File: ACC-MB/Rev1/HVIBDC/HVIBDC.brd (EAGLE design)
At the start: 100.2 x 48.2 mm, 34 parts, among them IC1 555

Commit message: update
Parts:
- added LED2, LED3, LED4, LED5: (no value), ACC-MB-R0:LED3MM
- added R13, R14, R15, R18: (no value), ACC-MB-R0:R0805
- moved U$2 9.06 mm to (-3.00, 17.0)
- moved U$14 6.79 mm to (0.70, 27.5), turned to 90 degrees
- moved U$1 1.00 mm to (66.0, 17.0)
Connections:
- new net N$17: LED2.K, R13.2
- new net N$19: LED3.K, R14.2
- new net N$25: LED4.K, R15.2
- new net N$27: LED5.K, R18.2
- net +12V: now also LED2.A, LED3.A, LED4.A, LED5.A
- net ACC_LGHT: now also R13.1
- net GND: now also R18.1
- net TSAL_GRN_GND: now also R14.1
- net TSAL_RED_GND: now also R15.1
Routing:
- net ACC_LGHT: track 50.5 -> 84.4 mm
- net TSAL_GRN_GND: track 73.5 -> 89.8 mm
- net TSAL_RED_GND: track 55.0 -> 68.1 mm
- net N$7: track 22.9 -> 34.6 mm
- net N$17: track 0.00 -> 8.95 mm
- net N$27: track 0.00 -> 5.57 mm
- net N$22: track 4.07 -> 8.62 mm
- net N$13: track 45.9 -> 50.0 mm
- net N$25: track 0.00 -> 3.74 mm
- net N$19: track 0.00 -> 3.32 mm
- net V-: track 58.9 -> 59.9 mm
- net V+: track 27.8 -> 28.8 mm
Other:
- board size 100.2 x 48.2 mm -> 92.2 x 49.2 mm

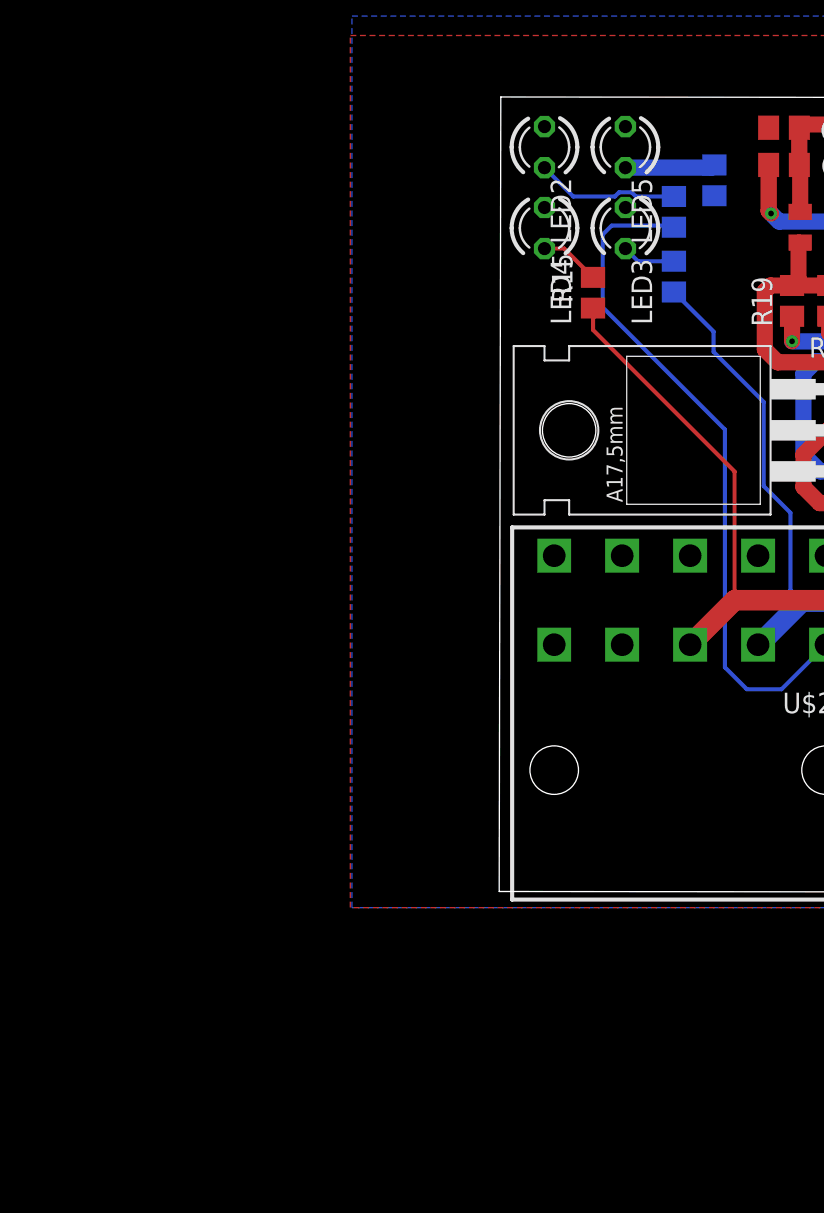
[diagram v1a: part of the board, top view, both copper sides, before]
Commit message: 7792 added to all DC
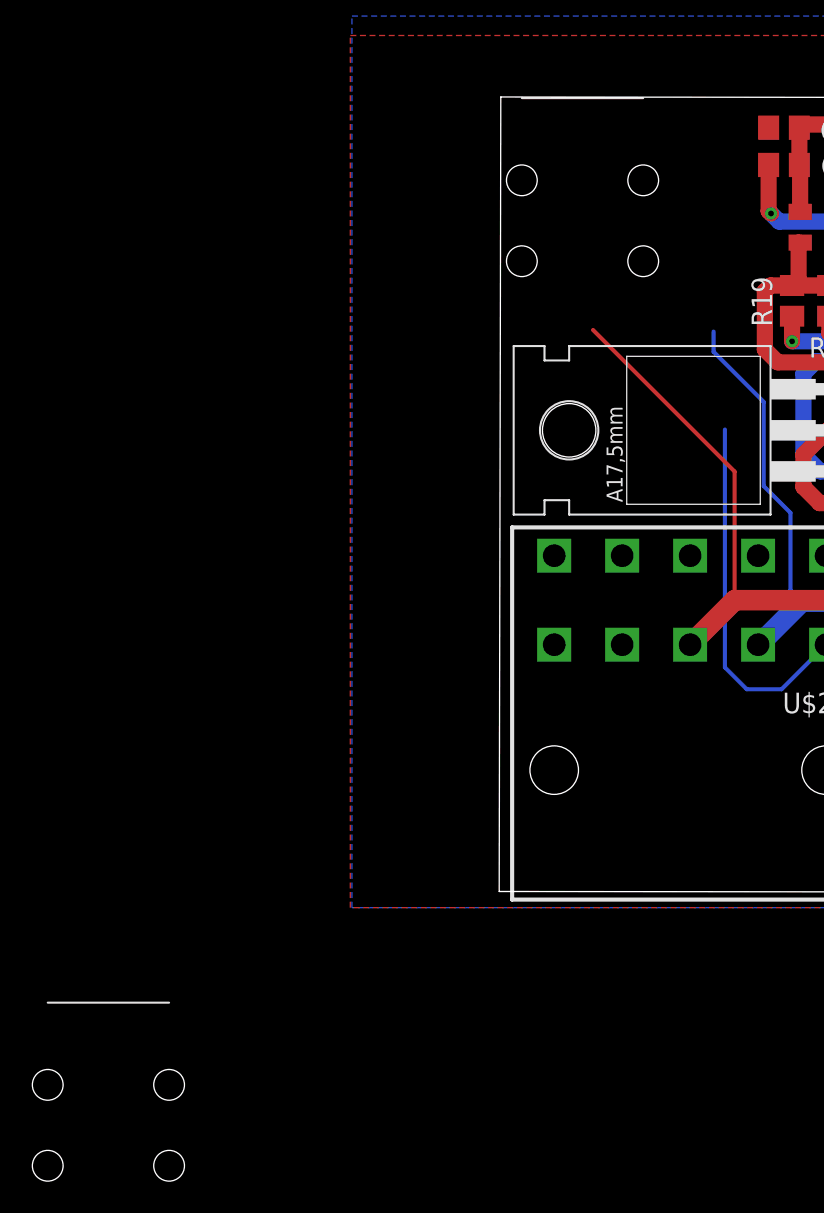
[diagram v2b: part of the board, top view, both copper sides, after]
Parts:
- removed LED2, LED3, LED4, LED5: (no value), ACC-MB-R0:LED3MM
- removed R13, R14, R15, R18: (no value), ACC-MB-R0:R0805
- added U$3, U$4: 7792, ACC-MB-R0:7792
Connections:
- removed net N$17: LED2.K, R13.2
- removed net N$19: LED3.K, R14.2
- removed net N$25: LED4.K, R15.2
- removed net N$27: LED5.K, R18.2
- net +12V: no longer LED2.A, LED3.A, LED4.A, LED5.A
- net ACC_LGHT: no longer R13.1
- net GND: no longer R18.1
- net TSAL_GRN_GND: no longer R14.1
- net TSAL_RED_GND: no longer R15.1
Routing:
- net ACC_LGHT: track 84.4 -> 64.5 mm
- net N$17: track 8.95 -> 0.00 mm
- net N$27: track 5.57 -> 0.00 mm
- net N$25: track 3.74 -> 0.00 mm
- net TSAL_GRN_GND: track 89.8 -> 86.3 mm
- net N$19: track 3.32 -> 0.00 mm
- net TSAL_RED_GND: track 68.1 -> 66.8 mm
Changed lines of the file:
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@@
 <drawing>
 <settings>
-<setting alwaysvectorfont="yes"/>
+<setting alwaysvectorfont="no"/>
 <setting verticaltext="up"/>
 </settings>
@@
 <element name="U$2" library="ACC-MB-R0" library_urn="urn:adsk.eagle:library:13208985" package="15-24-6100" package3d_urn="urn:adsk.eagle:package:14396594/2" value="15-24-6100" x="-3" y="17"/>
 <element name="U$1" library="ACC-MB-R0" library_urn="urn:adsk.eagle:library:13208985" package="15-24-6100" package3d_urn="urn:adsk.eagle:package:14396594/2" value="15-24-6100" x="66" y="17"/>
-<element name="LED2" library="ACC-MB-R0" library_urn="urn:adsk.eagle:library:13208985" package="LED3MM" package3d_urn="urn:adsk.eagle:package:15797/1" value="" x="-12" y="45" rot="R270"/>
-<element name="R13" library="ACC-MB-R0" library_urn="urn:adsk.eagle:library:13208985" package="R0805" package3d_urn="urn:adsk.eagle:package:13209583/1" value="" x="-4" y="41" rot="MR90">
-<attribute name="SPICEPREFIX" value="R" x="-4" y="41" size="1.778" layer="28" rot="MR90" display="off"/>
-</element>
-<element name="LED3" library="ACC-MB-R0" library_urn="urn:adsk.eagle:library:13208985" package="LED3MM" package3d_urn="urn:adsk.eagle:package:15797/1" value="" x="-7" y="40" rot="R270"/>
-<element name="R14" library="ACC-MB-R0" library_urn="urn:adsk.eagle:library:13208985" package="R0805" package3d_urn="urn:adsk.eagle:package:13209583/1" value="" x="-4" y="37" rot="MR90">
-<attribute name="SPICEPREFIX" value="R" x="-4" y="37" size="1.778" layer="28" rot="MR90" display="off"/>
-</element>
-<element name="LED4" library="ACC-MB-R0" library_urn="urn:adsk.eagle:library:13208985" package="LED3MM" package3d_urn="urn:adsk.eagle:package:15797/1" value="" x="-12" y="40" rot="R270"/>
-<element name="R15" library="ACC-MB-R0" library_urn="urn:adsk.eagle:library:13208985" package="R0805" package3d_urn="urn:adsk.eagle:package:13209583/1" value="" x="-9" y="36" rot="R90">
-<attribute name="SPICEPREFIX" value="R" x="-9" y="36" size="1.778" layer="27" rot="R90" display="off"/>
-</element>
-<element name="LED5" library="ACC-MB-R0" library_urn="urn:adsk.eagle:library:13208985" package="LED3MM" package3d_urn="urn:adsk.eagle:package:15797/1" value="" x="-7" y="45" rot="R270"/>
-<element name="R18" library="ACC-MB-R0" library_urn="urn:adsk.eagle:library:13208985" package="R0805" package3d_urn="urn:adsk.eagle:package:13209583/1" value="" x="-1.5" y="42.95" rot="MR90">
-<attribute name="SPICEPREFIX" value="R" x="-1.5" y="42.95" size="1.778" layer="28" rot="MR90" display="off"/>
-</element>
+<element name="U$3" library="ACC-MB-R0" library_urn="urn:adsk.eagle:library:13208985" package="7792" package3d_urn="urn:adsk.eagle:package:14511284/2" value="7792" x="-42.7" y="-17.95"/>
+<element name="U$4" library="ACC-MB-R0" library_urn="urn:adsk.eagle:library:13208985" package="7792" package3d_urn="urn:adsk.eagle:package:14511284/2" value="7792" x="-13.4" y="37.95"/>
 </elements>
 <signals>
@@
 <wire x1="13.9" y1="33" x2="14.19" y2="33.29" width="1" layer="16"/>
 <contactref element="U$2" pad="7"/>
-<contactref element="R18" pad="1"/>
-<wire x1="1.2" y1="19.75" x2="-1.5" y2="42" width="0" layer="19" extent="1-1"/>
-<wire x1="7.05" y1="30.04" x2="1.2" y2="19.75" width="0" layer="19" extent="1-1"/>
-<wire x1="5.5" y1="33" x2="7.05" y2="30.04" width="0" layer="19" extent="16-16"/>
+<wire x1="30.7" y1="45.05" x2="41.4" y2="40" width="0" layer="19" extent="1-16"/>
+<wire x1="28" y1="44.95" x2="30.7" y2="45.05" width="0" layer="19" extent="1-1"/>
+<wire x1="25.05" y1="44.95" x2="28" y2="44.95" width="0" layer="19" extent="1-1"/>
+<wire x1="22" y1="44.95" x2="25.05" y2="44.95" width="0" layer="19" extent="1-1"/>
+<wire x1="19" y1="44.95" x2="22" y2="44.95" width="0" layer="19" extent="1-1"/>
+<wire x1="11.08" y1="36.4" x2="19" y2="44.95" width="0" layer="19" extent="1-16"/>
 <wire x1="7.8" y1="34.55" x2="7.6" y2="35.1" width="0" layer="19" extent="1-16"/>
 <wire x1="1.85" y1="46.2" x2="1.85" y2="43.9" width="0" layer="19" extent="1-1"/>
+<wire x1="7.05" y1="30.04" x2="5.5" y2="33" width="0" layer="19" extent="16-16"/>
 <wire x1="13.86" y1="29.05" x2="13.9" y2="33" width="0" layer="19" extent="16-16"/>
 <wire x1="24.81" y1="29.15" x2="13.86" y2="29.05" width="0" layer="19" extent="1-1"/>
-<wire x1="19" y1="44.95" x2="11.08" y2="36.4" width="0" layer="19" extent="1-16"/>
-<wire x1="22" y1="44.95" x2="19" y2="44.95" width="0" layer="19" extent="1-1"/>
-<wire x1="25.05" y1="44.95" x2="22" y2="44.95" width="0" layer="19" extent="1-1"/>
-<wire x1="28" y1="44.95" x2="25.05" y2="44.95" width="0" layer="19" extent="1-1"/>
-<wire x1="30.7" y1="45.05" x2="28" y2="44.95" width="0" layer="19" extent="1-1"/>
-<wire x1="41.4" y1="40" x2="30.7" y2="45.05" width="0" layer="19" extent="1-16"/>
+<wire x1="1.2" y1="19.75" x2="7.05" y2="30.04" width="0" layer="19" extent="1-1"/>
 <wire x1="41.46" y1="21.35" x2="24.81" y2="29.15" width="0" layer="19" extent="1-1"/>
 </signal>
@@
 <contactref element="U$2" pad="9"/>
 <contactref element="U$2" pad="10"/>
-<contactref element="LED5" pad="A"/>
-<contactref element="LED4" pad="A"/>
-<contactref element="LED3" pad="A"/>
-<contactref element="LED2" pad="A"/>
-<wire x1="-12" y1="41.27" x2="-7" y2="46.27" width="0" layer="19" extent="1-1"/>
-<wire x1="-7" y1="41.27" x2="-12" y2="41.27" width="0" layer="19" extent="1-1"/>
-<wire x1="-12" y1="46.27" x2="-7" y2="41.27" width="0" layer="19" extent="1-1"/>
-<wire x1="-11.4" y1="19.75" x2="-12" y2="46.27" width="0" layer="19" extent="1-1"/>
-<wire x1="-7.2" y1="19.75" x2="-11.4" y2="19.75" width="0" layer="19" extent="1-1"/>
-<wire x1="-3" y1="19.75" x2="-7.2" y2="19.75" width="0" layer="19" extent="1-1"/>
-<wire x1="9.9" y1="36.45" x2="-3" y2="19.75" width="0" layer="19" extent="1-1"/>
-<wire x1="10.65" y1="43.05" x2="9.1" y2="38.4" width="0" layer="19" extent="1-1"/>
-<wire x1="48" y1="32" x2="48.19" y2="26.23465625" width="0" layer="19" extent="1-16"/>
+<wire x1="48.19" y1="26.23465625" x2="48" y2="32" width="0" layer="19" extent="1-16"/>
+<wire x1="9.1" y1="38.4" x2="10.65" y2="43.05" width="0" layer="19" extent="1-1"/>
 <wire x1="21.81" y1="33.29" x2="14.19" y2="40.91" width="0" layer="19" extent="1-1"/>
+<wire x1="-3" y1="19.75" x2="9.9" y2="36.45" width="0" layer="19" extent="1-1"/>
+<wire x1="-7.2" y1="19.75" x2="-3" y2="19.75" width="0" layer="19" extent="1-1"/>
+<wire x1="-11.4" y1="19.75" x2="-7.2" y2="19.75" width="0" layer="19" extent="1-1"/>
 </signal>
 <signal name="AIR_ON">
@@
 <wire x1="16.4" y1="29.05" x2="16.4" y2="23.4" width="1.27" layer="16"/>
 <wire x1="1.25" y1="14.25" x2="1.2" y2="14.25" width="1.27" layer="16"/>
-<contactref element="R14" pad="1"/>
 <wire x1="3.9126" y1="16.9126" x2="3.2" y2="17.6252" width="0.254" layer="16"/>
 <wire x1="3.2" y1="17.6252" x2="3.2" y2="22.4" width="0.254" layer="16"/>
@@
 <wire x1="1.55" y1="24.05" x2="1.55" y2="29.25" width="0.254" layer="16"/>
 <wire x1="-1.55" y1="32.35" x2="-1.55" y2="33.6" width="0.254" layer="16"/>
-<wire x1="-1.55" y1="33.6" x2="-4" y2="36.05" width="0.254" layer="16"/>
 </signal>
 <signal name="ACC_LGHT" class="1">
@@
 <wire x1="40.24715" y1="17" x2="13.15" y2="17" width="1.27" layer="16"/>
 <wire x1="10.4" y1="14.25" x2="5.4" y2="14.25" width="1.27" layer="16"/>
-<contactref element="R13" pad="1"/>
 <wire x1="5.4" y1="14.25" x2="2.65" y2="11.5" width="0.254" layer="16"/>
 <wire x1="0.5" y1="11.5" x2="-0.85" y2="12.85" width="0.254" layer="16"/>
 <wire x1="-0.85" y1="12.85" x2="-0.85" y2="27.55" width="0.254" layer="16"/>
-<wire x1="-8.4" y1="35.1" x2="-8.4" y2="39.6" width="0.254" layer="16"/>
-<wire x1="-8.4" y1="39.6" x2="-7.85" y2="40.15" width="0.254" layer="16"/>
-<wire x1="-4.1" y1="40.15" x2="-4" y2="40.05" width="0.254" layer="16"/>
 <wire x1="2.65" y1="11.5" x2="0.5" y2="11.5" width="0.254" layer="16"/>
-<wire x1="-0.85" y1="27.55" x2="-8.4" y2="35.1" width="0.254" layer="16"/>
-<wire x1="-7.85" y1="40.15" x2="-4.1" y2="40.15" width="0.254" layer="16"/>
 </signal>
 <signal name="TSAL_RED_GND" class="1">
@@
 <wire x1="37.25" y1="22.25" x2="37.25" y2="25.15" width="1.27" layer="1"/>
 <wire x1="-0.25" y1="17" x2="32" y2="17" width="1.27" layer="1"/>
-<contactref element="R15" pad="1"/>
-<wire x1="-9" y1="35.05" x2="-9" y2="33.7" width="0.254" layer="1"/>
 <wire x1="-0.25" y1="24.95" x2="-0.25" y2="17" width="0.254" layer="1"/>
 <wire x1="-9" y1="33.7" x2="-0.25" y2="24.95" width="0.254" layer="1"/>
@@
 <contactref element="U$2" pad="6"/>
 </signal>
-<signal name="N$17" class="1">
-<contactref element="R13" pad="2"/>
-<contactref element="LED2" pad="K"/>
-<wire x1="-10.22" y1="41.95" x2="-12" y2="43.73" width="0.254" layer="16"/>
-<wire x1="-4" y1="41.95" x2="-6.35091875" y2="41.95" width="0.254" layer="16"/>
-<wire x1="-6.35091875" y1="41.95" x2="-6.61071875" y2="42.2098" width="0.254" layer="16"/>
-<wire x1="-6.61071875" y1="42.2098" x2="-7.38928125" y2="42.2098" width="0.254" layer="16"/>
-<wire x1="-7.38928125" y1="42.2098" x2="-7.64908125" y2="41.95" width="0.254" layer="16"/>
-<wire x1="-7.64908125" y1="41.95" x2="-10.22" y2="41.95" width="0.254" layer="16"/>
-</signal>
-<signal name="N$19" class="1">
-<contactref element="R14" pad="2"/>
-<contactref element="LED3" pad="K"/>
-<wire x1="-4" y1="37.95" x2="-6.22" y2="37.95" width="0.254" layer="16"/>
-<wire x1="-6.22" y1="37.95" x2="-7" y2="38.73" width="0.254" layer="16"/>
-</signal>
-<signal name="N$25" class="1">
-<contactref element="R15" pad="2"/>
-<contactref element="LED4" pad="K"/>
-<wire x1="-9" y1="36.95" x2="-10.78" y2="38.73" width="0.254" layer="1"/>
-<wire x1="-10.78" y1="38.73" x2="-12" y2="38.73" width="0.254" layer="1"/>
-</signal>
-<signal name="N$27">
-<contactref element="R18" pad="2"/>
-<contactref element="LED5" pad="K"/>
-<wire x1="-7" y1="43.73" x2="-1.67" y2="43.73" width="1" layer="16"/>
-<wire x1="-1.67" y1="43.73" x2="-1.5" y2="43.9" width="1" layer="16"/>
-</signal>
 </signals>
